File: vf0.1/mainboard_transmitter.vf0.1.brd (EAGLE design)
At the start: 100 x 80 mm, 10 parts, among them J1 AUDIO-JACK2PTH, Y1 16MHz

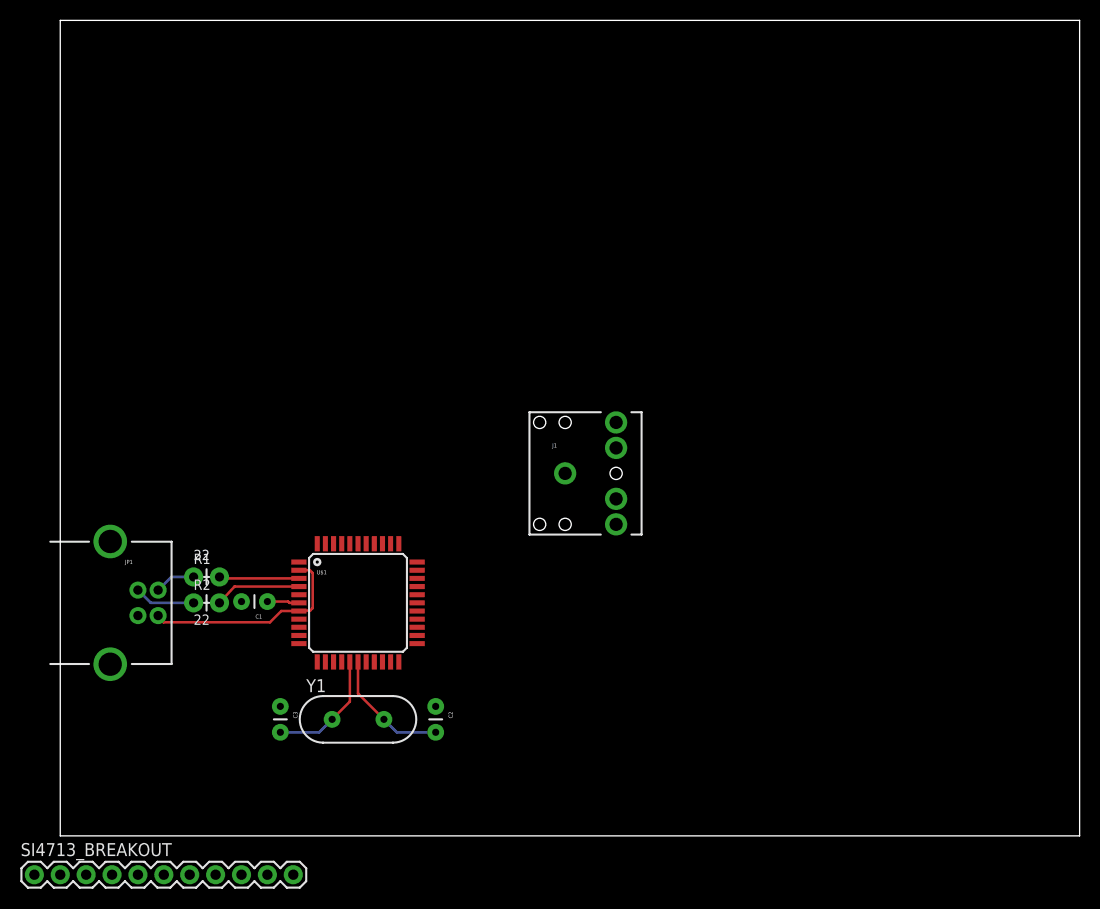
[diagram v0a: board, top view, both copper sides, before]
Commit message: Mostly complete, routed audio, FM transmitter, data transmitter
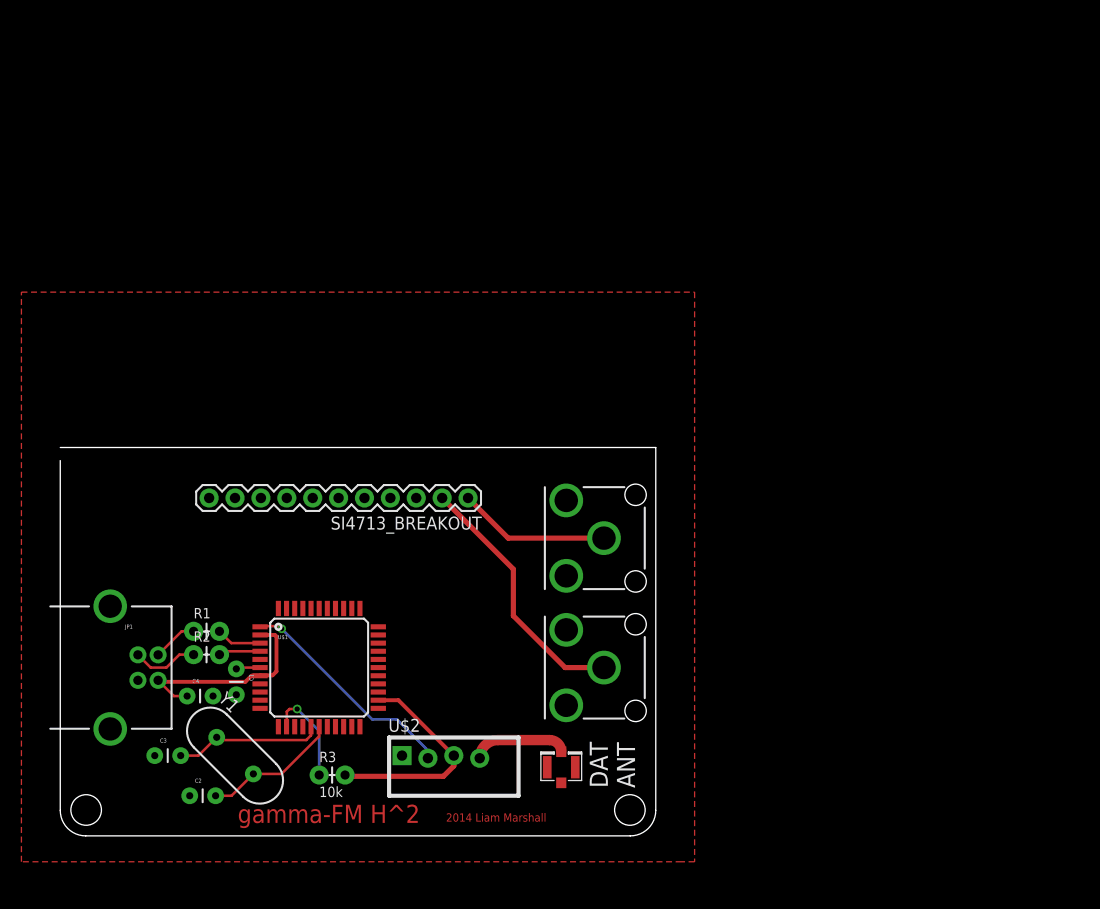
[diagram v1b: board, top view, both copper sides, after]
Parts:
- removed J1: AUDIO-JACK2PTH, SparkFun-Connectors:AUDIO-JACK
- added C4: 1uF, SparkFun-Capacitors:CAP-PTH-SMALL
- added J2: U.FL, SparkFun-Connectors:U.FL
- added L, R: RCA, SparkFun-Connectors:RCA
- added R3: 10k, SparkFun-Resistors:AXIAL-0.1
- added U$2: RF-LINK_TX, SparkFun-RF:RF-LINK_TX
- moved SI4713_BREAKOUT 56.4 mm to (40.0, 33.1), turned to 180 degrees
- moved C2 25.7 mm to (12.7, 3.94), turned to 0 degrees
- moved C3 13.2 mm to (9.27, 7.87), turned to 0 degrees
- moved Y1 12.6 mm to (17.1, 7.87), turned to 315 degrees
- moved U$1 7.41 mm to (25.4, 16.5)
- moved C1 7.27 mm to (17.3, 16.4), turned to 270 degrees
- moved JP1 6.35 mm to (7.62, 16.5)
- moved R1 5.33 mm to (13.1, 20.1)
- moved R2 5.08 mm to (13.1, 17.8)
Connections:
- new net N$8: R3.P$1, U$1.13
- new net N$9: J2.P$3, U$2.ANT
- new net RADIODAT: U$1.1, U$2.DATA
- new net SCL: SI4713_BREAKOUT.9, U$1.18
- new net SDA: SI4713_BREAKOUT.8, U$1.19
- new net T_RST: SI4713_BREAKOUT.11, U$1.26
- net GND: now also C4.2, J2.P$1, J2.P$2, L.PIN, R.PIN, SI4713_BREAKOUT.4, U$2.GND; no longer J1.SLEEVE
- net L: now also L.SHELL, SI4713_BREAKOUT.2; no longer J1.TIP
- net R: now also R.SHELL, SI4713_BREAKOUT.1; no longer J1.RING
- net UVCC: now also C4.1
- net VCC: now also R3.P$2, SI4713_BREAKOUT.3, U$1.14, U$1.24, U$1.34, U$1.44, U$2.VCC
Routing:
- net L: track 0.00 -> 25.4 mm
- net RADIODAT: track 0.00 -> 22.3 mm, vias 0 -> 1
- net VCC: track 0.00 -> 21.8 mm
- net R: track 0.00 -> 15.0 mm
- net N$8: track 0.00 -> 9.98 mm, vias 0 -> 1
- net N$9: track 0.00 -> 9.21 mm
- net N$4: track 8.49 -> 4.12 mm
- net N$3: track 7.85 -> 4.46 mm
- net N$7: track 12.0 -> 14.7 mm
- net N$6: track 12.3 -> 13.5 mm
- net N$5: track 3.14 -> 2.38 mm
- net N$1: track 5.98 -> 6.50 mm
- added copper zone on layer 1, net GND
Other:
- board size 100 x 80 mm -> 58.4 x 38.1 mm
- board text added: "2014 Liam Marshall"
- board text added: "DAT ANT"
- board text added: "gamma-FM H^2"

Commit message: Final revision of vf0.1
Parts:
- removed J2: U.FL, SparkFun-Connectors:U.FL
- added J$1: SMA_EDGE, SparkFun-Connectors:SMA-EDGE
- moved C2 12.5 mm to (25.1, 2.79)
- moved C3 11.9 mm to (20.1, 2.79)
- moved Y1 8.10 mm to (25.1, 6.60), turned to 0 degrees
- moved C1 5.96 mm to (19.9, 11.0), turned to 180 degrees
- moved R3 5.01 mm to (22.9, 10.3), turned to 90 degrees
- moved U$1 4.91 mm to (30.0, 18.3)
- moved R1 4.71 mm to (17.8, 20.3)
- moved C4 4.71 mm to (17.1, 14.0)
- moved R2 4.71 mm to (17.8, 18.0)
- moved JP1 4.71 mm to (12.3, 16.8)
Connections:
- removed net UVCC: C4.1, JP1.VBUS, U$1.2, U$1.7
- net GND: now also J$1.GND@0, J$1.GND@1, J$1.GND@2, J$1.GND@3; no longer J2.P$1, J2.P$2
- net N$9: now also J$1.SIG; no longer J2.P$3
- net VCC: now also C4.1, JP1.VBUS, U$1.2, U$1.7
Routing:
- net VCC: track 21.8 -> 80.4 mm
- net T_RST: track 0.00 -> 30.1 mm, vias 0 -> 2
- net SCL: track 0.00 -> 26.2 mm, vias 0 -> 1
- net SDA: track 0.00 -> 24.6 mm, vias 0 -> 1
- net UVCC: track 20.7 -> 0.00 mm
- net GND: track 0.00 -> 14.4 mm, vias 0 -> 5
- net N$5: track 2.38 -> 9.76 mm, vias 0 -> 1
- net N$9: track 9.21 -> 16.0 mm
- net N$8: track 9.98 -> 5.55 mm, vias 1 -> 0
- net N$6: track 13.5 -> 10.6 mm
- net RADIODAT: track 22.3 -> 20.7 mm
- net N$7: track 14.7 -> 13.4 mm
- net N$4: track 4.12 -> 4.62 mm
- added copper zone on layer 16, net GND
- removed copper zone on layer 1, net GND
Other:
- board size 58.4 x 38.1 mm -> 55.9 x 40.6 mm
- board text added: ">DRAWING_NAME"

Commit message: Finalized transmitter main board
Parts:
- added J1: AVR_SPI_PRG_6TESTPOINTS, SparkFun-Connectors:2X3_TEST_POINTS
- moved SI4713_BREAKOUT 25.4 mm to (14.6, 33.7), turned to 0 degrees
- moved J$1 6.99 mm to (50.0, 4.83)
- moved L 5.08 mm to (48.3, 16.5)
- moved R 5.08 mm to (48.3, 29.2)
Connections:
- removed net N$8: R3.P$1, U$1.13
- new net !RESET: J1.5, R3.P$1, U$1.13
- new net MISO: J1.1, U$1.10
- new net MOSI: J1.4, U$1.11
- new net SCK: J1.3, U$1.9
- net GND: now also J1.6
- net RADIODAT: now also U$1.25; no longer U$1.1
- net VCC: now also J1.2
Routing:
- net R: track 14.9 -> 42.2 mm
- net L: track 25.3 -> 51.8 mm
- net MOSI: track 0.00 -> 13.9 mm
- net !RESET: track 0.00 -> 12.5 mm, vias 0 -> 1
- net T_RST: track 30.1 -> 19.2 mm, vias 2 -> 0
- net RADIODAT: track 20.7 -> 12.7 mm
- net MISO: track 0.00 -> 7.03 mm
- net N$9: track 16.0 -> 9.00 mm
- net SCK: track 0.00 -> 5.66 mm
- net N$8: track 5.55 -> 0.00 mm
- net GND: track 14.4 -> 19.0 mm, vias 5 -> 4
- net SCL: track 26.2 -> 30.2 mm
- net SDA: track 24.6 -> 27.2 mm
- net VCC: track 80.4 -> 82.0 mm
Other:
- board size 55.9 x 40.6 mm -> 48.9 x 38.1 mm
- board text added: "DAT"
- board text removed: ">DRAWING_NAME"
- board text removed: "DAT ANT"
